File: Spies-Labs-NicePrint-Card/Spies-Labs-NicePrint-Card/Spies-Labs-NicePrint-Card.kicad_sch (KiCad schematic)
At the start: 27 parts, among them J1 Conn_02x13, J2 AppleIIBus, SW1 SW_DIP_x04, U1 74LS374, U10 74LS02, U11 74LS174, U12 74LS30, U13 74LS138, U2 74LS374, U3 74LS279, U4 27C64, U5 27C64, U6 74LS00, U7 27C64, U8 74LS138, U9 2114

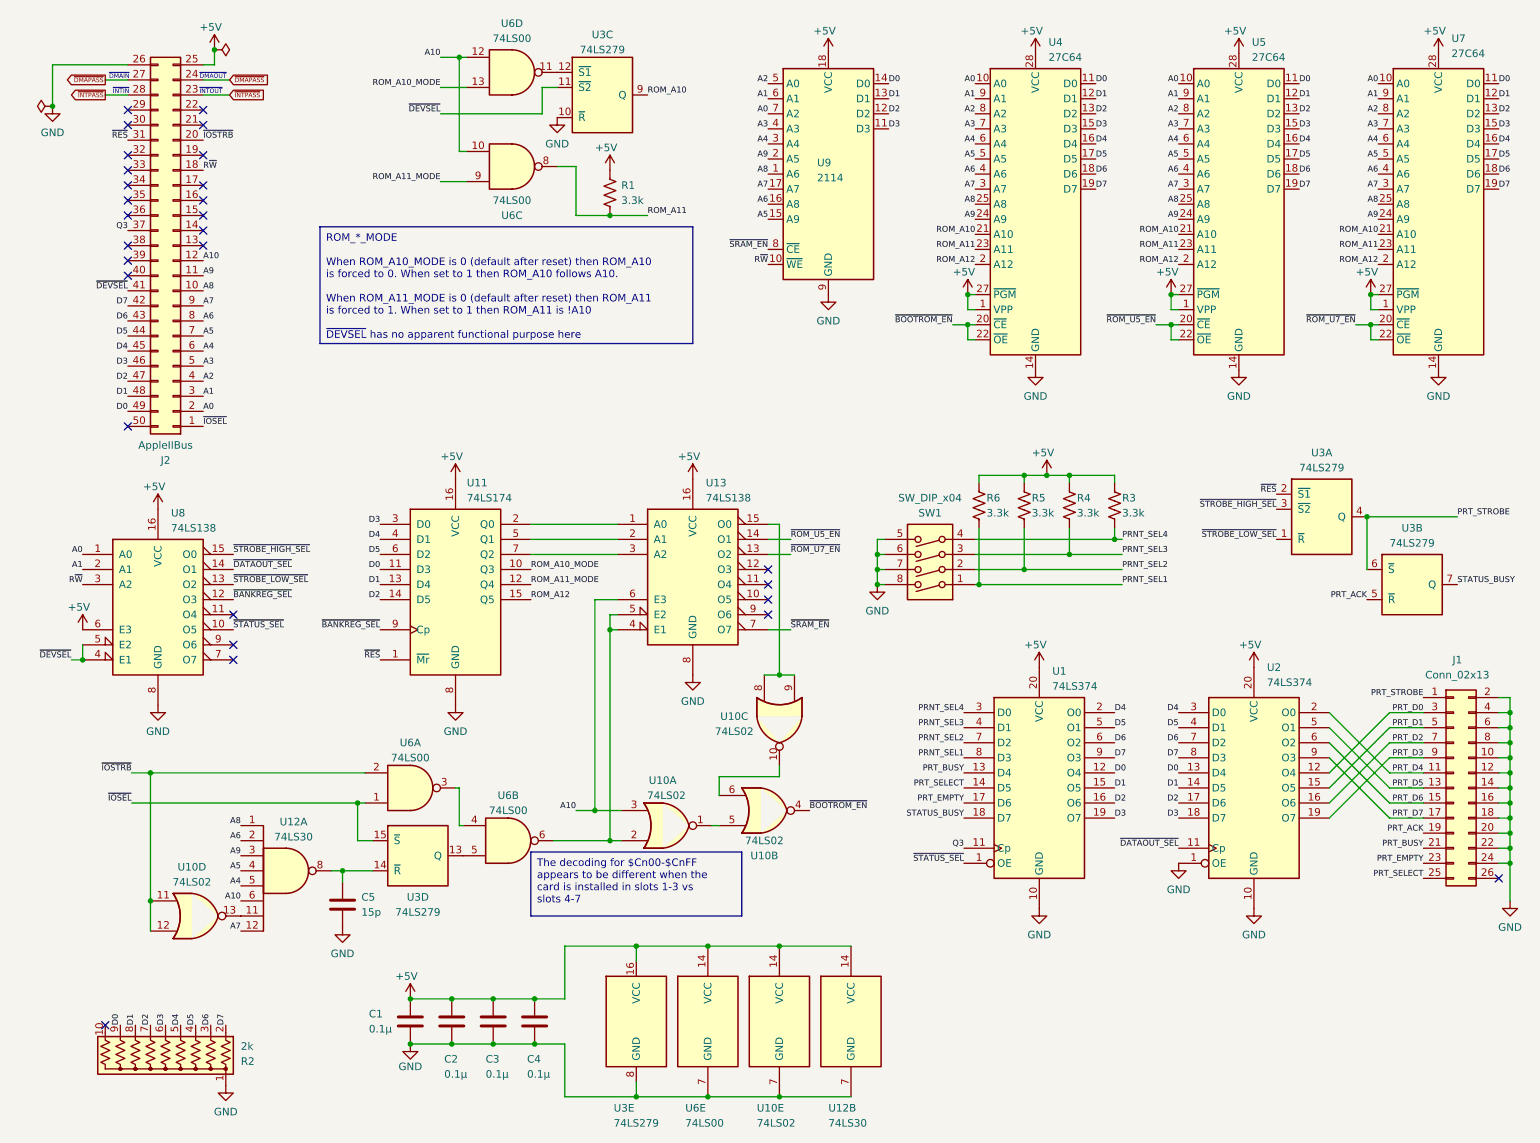
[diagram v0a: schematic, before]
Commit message: Update Spies Niceprint card to kicad 8 and the shared symbol library
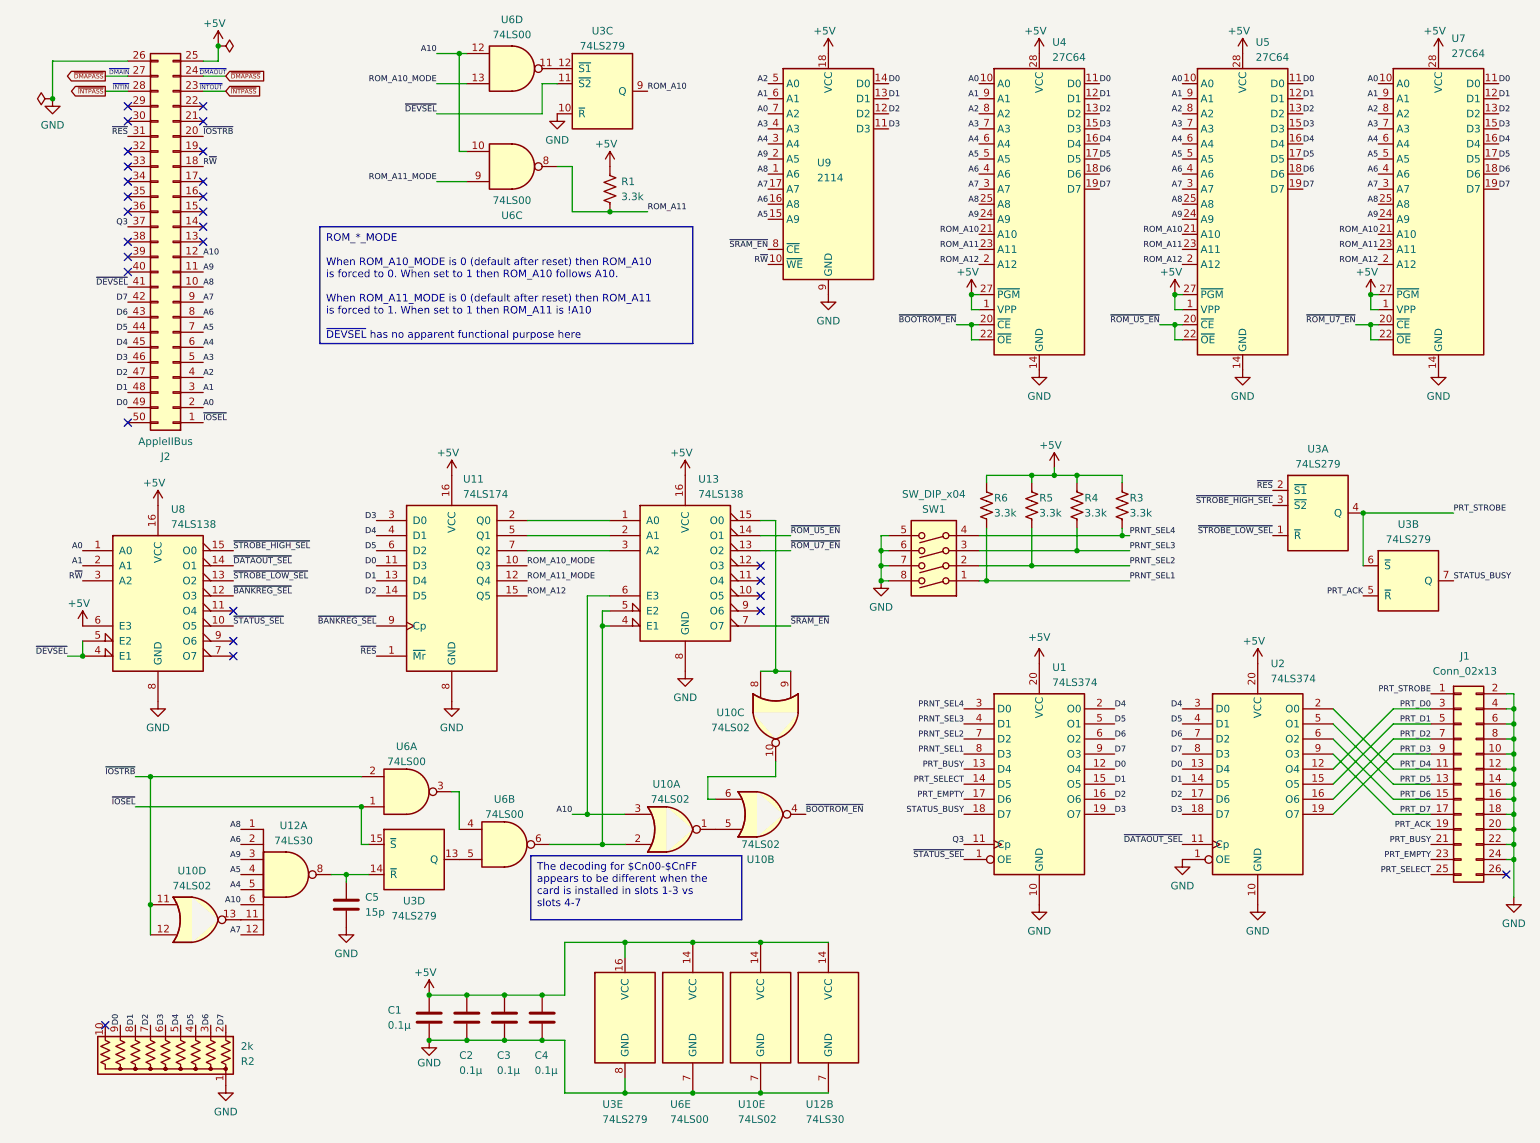
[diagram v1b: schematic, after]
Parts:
- J2: footprint Apple:AppleIIBus_Edge -> (none)
- U3: symbol Logic:74LS279 -> Logic_Legacy:74LS279
- U9: symbol Memory:2114 -> Memory_Legacy:2114
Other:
- moved on the sheet: C1, C2, C3, C4, C5, J1, J2, R1, R3, R4, R5, R6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
